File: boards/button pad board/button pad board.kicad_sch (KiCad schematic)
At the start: 4 parts

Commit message: button schematic work
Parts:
- added D1: LED_RBGA, LED_SMD:LED_RGB_5050-6, symbol Device:LED_RBGA
- U1: Mouser (none) -> 474-COM-07836
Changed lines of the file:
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@@
+      (effects (font (size 1.27 1.27)) hide)
+    )
+    (property "Mouser" "474-COM-07836 " (at 57.15 39.37 0)
       (effects (font (size 1.27 1.27)) hide)
     )
@@
       (effects (font (size 1.27 1.27)) hide)
     )
+    (property "Mouser" "474-COM-07836 " (at 30.48 39.37 0)
+      (effects (font (size 1.27 1.27)) hide)
+    )
     (pin "B1")
     (pin "G1")
@@
       (effects (font (size 1.27 1.27)) hide)
     )
+    (property "Mouser" "474-COM-07836 " (at 29.21 74.93 0)
+      (effects (font (size 1.27 1.27)) hide)
+    )
     (pin "B1")
     (pin "G1")
@@
       (effects (font (size 1.27 1.27)) hide)
     )
+    (property "Mouser" "474-COM-07836 " (at 55.88 74.93 0)
+      (effects (font (size 1.27 1.27)) hide)
+    )
     (pin "B1")
     (pin "G1")
@@
         )
       )
+    )
+  )
+  (symbol (lib_id "Device:LED_RBGA") (at 52.07 129.54 0) (unit 1)
+    (in_bom yes) (on_board yes) (dnp no) (fields_autoplaced)
+    (property "Reference" "D1" (at 52.07 116.84 0)
+      (effects (font (size 1.27 1.27)))
+    )
+    (property "Value" "LED_RBGA" (at 52.07 119.38 0)
+      (effects (font (size 1.27 1.27)))
+    )
+    (property "Footprint" "LED_SMD:LED_RGB_5050-6" (at 52.07 130.81 0)
+      (effects (font (size 1.27 1.27)) hide)
+    )
+    (property "Datasheet" "~" (at 52.07 130.81 0)
+      (effects (font (size 1.27 1.27)) hide)
+    )
+    (property "LCSC" "C784540" (at 52.07 129.54 0)
+      (effects (font (size 1.27 1.27)) hide)
+    )
+    (pin "1")
+    (pin "2")
+    (pin "3")
+    (pin "4")
+    (instances
+      (project "button pad board"
+        (path "/66d98af2-097e-4f68-99f2-351c9b9568f9"
+          (reference "D1") (unit 1)
+        )
+      )

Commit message: worked on the button board a bit
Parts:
- D1: footprint LED_SMD:LED_RGB_5050-6 -> yarrboard:WURTH_LED_RGB_5050-6; symbol Device:LED_RBGA -> yarrboard:LED_RGB; Mouser (none) -> 710-150505M173300
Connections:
- net B0: now also D1.BK
- net G0: now also D1.GK
- net R0: now also D1.RK
- net VCC: now also D1.BA, D1.GA, D1.RA
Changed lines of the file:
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@@
 (kicad_sch (version 20230121) (generator eeschema)
   (paper "A4")
+  (junction (at 60.96 123.19) (diameter 0) (color 0 0 0 0)
+  )
+  (junction (at 60.96 128.27) (diameter 0) (color 0 0 0 0)
+  )
+  (wire (pts (xy 60.96 123.19) (xy 60.96 128.27))
+    (stroke (width 0) (type default))
+  )
   (wire (pts (xy 238.76 71.12) (xy 238.76 74.93))
     (stroke (width 0) (type default))
@@
     (stroke (width 0) (type default))
   )
+  (wire (pts (xy 58.42 123.19) (xy 60.96 123.19))
+    (stroke (width 0) (type default))
+  )
   (wire (pts (xy 238.76 74.93) (xy 234.95 74.93))
     (stroke (width 0) (type default))
@@
     (stroke (width 0) (type default))
   )
+  (wire (pts (xy 44.45 128.27) (xy 48.26 128.27))
+    (stroke (width 0) (type default))
+  )
   (wire (pts (xy 119.38 53.34) (xy 121.92 53.34))
     (stroke (width 0) (type default))
@@
     (stroke (width 0) (type default))
   )
+  (wire (pts (xy 60.96 128.27) (xy 58.42 128.27))
+    (stroke (width 0) (type default))
+  )
+  (wire (pts (xy 60.96 133.35) (xy 60.96 128.27))
+    (stroke (width 0) (type default))
+  )
+  (wire (pts (xy 44.45 133.35) (xy 48.26 133.35))
+    (stroke (width 0) (type default))
+  )
   (wire (pts (xy 154.94 35.56) (xy 154.94 39.37))
     (stroke (width 0) (type default))
@@
     (stroke (width 0) (type default))
   )
+  (wire (pts (xy 44.45 123.19) (xy 48.26 123.19))
+    (stroke (width 0) (type default))
+  )
   (wire (pts (xy 209.55 53.34) (xy 212.09 53.34))
     (stroke (width 0) (type default))
@@
     (stroke (width 0) (type default))
   )
+  (wire (pts (xy 60.96 120.65) (xy 60.96 123.19))
+    (stroke (width 0) (type default))
+  )
   (wire (pts (xy 96.52 39.37) (xy 92.71 39.37))
     (stroke (width 0) (type default))
@@
     (stroke (width 0) (type default))
   )
+  (wire (pts (xy 58.42 133.35) (xy 60.96 133.35))
+    (stroke (width 0) (type default))
+  )
   (wire (pts (xy 181.61 39.37) (xy 177.8 39.37))
     (stroke (width 0) (type default))
@@
     )
   )
+  (global_label "G0" (shape input) (at 44.45 128.27 180) (fields_autoplaced)
+    (effects (font (size 1.27 1.27)) (justify right))
+    (property "Intersheetrefs" "${INTERSHEET_REFS}" (at 38.9853 128.27 0)
+      (effects (font (size 1.27 1.27)) (justify right) hide)
+    )
+  )
   (global_label "IN1" (shape input) (at 167.64 53.34 180) (fields_autoplaced)
     (effects (font (size 1.27 1.27)) (justify right))
@@
     )
   )
+  (global_label "B0" (shape input) (at 44.45 133.35 180) (fields_autoplaced)
+    (effects (font (size 1.27 1.27)) (justify right))
+    (property "Intersheetrefs" "${INTERSHEET_REFS}" (at 38.9853 133.35 0)
+      (effects (font (size 1.27 1.27)) (justify right) hide)
+    )
+  )
   (global_label "G1" (shape input) (at 226.06 39.37 180) (fields_autoplaced)
     (effects (font (size 1.27 1.27)) (justify right))
@@
     (effects (font (size 1.27 1.27)) (justify right))
     (property "Intersheetrefs" "${INTERSHEET_REFS}" (at 135.5053 34.29 0)
+      (effects (font (size 1.27 1.27)) (justify right) hide)
+    )
+  )
+  (global_label "R0" (shape input) (at 44.45 123.19 180) (fields_autoplaced)
+    (effects (font (size 1.27 1.27)) (justify right))
+    (property "Intersheetrefs" "${INTERSHEET_REFS}" (at 38.9853 123.19 0)
       (effects (font (size 1.27 1.27)) (justify right) hide)
     )
@@
     )
   )
+  (symbol (lib_id "power:VCC") (at 60.96 120.65 0) (unit 1)
+    (in_bom yes) (on_board yes) (dnp no) (fields_autoplaced)
+    (property "Reference" "#PWR033" (at 60.96 124.46 0)
+      (effects (font (size 1.27 1.27)) hide)
+    )
+    (property "Value" "VCC" (at 60.96 115.57 0)
+      (effects (font (size 1.27 1.27)))
+    )
+    (property "Footprint" "" (at 60.96 120.65 0)
+      (effects (font (size 1.27 1.27)) hide)
+    )
+    (property "Datasheet" "" (at 60.96 120.65 0)
+      (effects (font (size 1.27 1.27)) hide)
+    )
+    (pin "1")
+    (instances
+      (project "button pad board"
+        (path "/66d98af2-097e-4f68-99f2-351c9b9568f9"
+          (reference "#PWR033") (unit 1)
+        )
+      )
+    )
+  )
   (symbol (lib_name "2x2_RGB_Button_1") (lib_id "yarrboard:2x2_RGB_Button") (at 87.63 39.37 0) (unit 1)
     (in_bom yes) (on_board yes) (dnp no) (fields_autoplaced)
@@
     )
   )
-  (symbol (lib_id "Device:LED_RBGA") (at 52.07 129.54 0) (unit 1)
-    (in_bom yes) (on_board yes) (dnp no) (fields_autoplaced)
-    (property "Reference" "D1" (at 52.07 116.84 0)
-      (effects (font (size 1.27 1.27)))
-    )
-    (property "Value" "LED_RBGA" (at 52.07 119.38 0)
-      (effects (font (size 1.27 1.27)))
-    )
-    (property "Footprint" "LED_SMD:LED_RGB_5050-6" (at 52.07 130.81 0)
-      (effects (font (size 1.27 1.27)) hide)
-    )
-    (property "Datasheet" "~" (at 52.07 130.81 0)
-      (effects (font (size 1.27 1.27)) hide)
-    )
-    (property "LCSC" "C784540" (at 52.07 129.54 0)
-      (effects (font (size 1.27 1.27)) hide)
-    )
-    (pin "1")
-    (pin "2")
-    (pin "3")
-    (pin "4")
-    (instances
-      (project "button pad board"
+  (symbol (lib_id "yarrboard:LED_RGB") (at 53.34 128.27 0) (unit 1)
+    (in_bom yes) (on_board yes) (dnp no) (fields_autoplaced)
+    (property "Reference" "D1" (at 53.34 115.57 0)
+      (effects (font (size 1.27 1.27)))
+    )
+    (property "Value" "LED_RBGA" (at 53.34 118.11 0)
+      (effects (font (size 1.27 1.27)))
+    )
+    (property "Footprint" "yarrboard:WURTH_LED_RGB_5050-6" (at 53.34 129.54 0)
+      (effects (font (size 1.27 1.27)) hide)
+    )
+    (property "Datasheet" "~" (at 53.34 129.54 0)
+      (effects (font (size 1.27 1.27)) hide)
+    )
+    (property "LCSC" "C784540" (at 53.34 128.27 0)
+      (effects (font (size 1.27 1.27)) hide)
+    )
+    (property "Mouser" " 710-150505M173300 " (at 53.34 128.27 0)
+      (effects (font (size 1.27 1.27)) hide)
+    )
+    (pin "BA")
+    (pin "BK")
+    (pin "GA")
+    (pin "GK")
+    (pin "RA")
+    (pin "RK")
+    (instances
+      (project "button pad board"

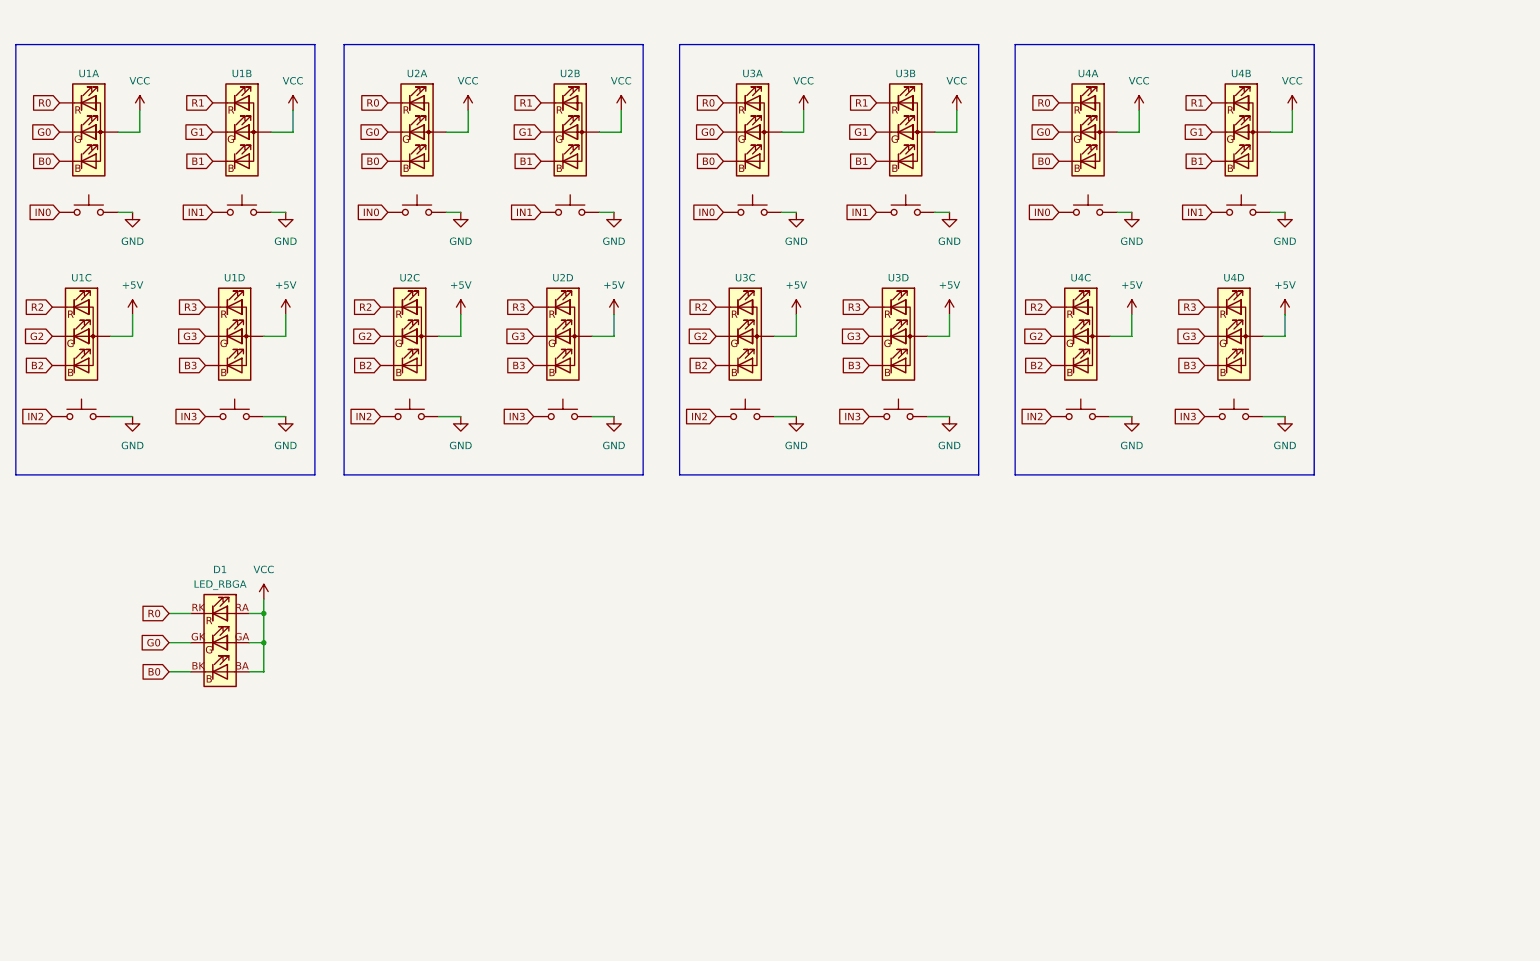
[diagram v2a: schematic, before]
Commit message: changed to 5050 led for interface board
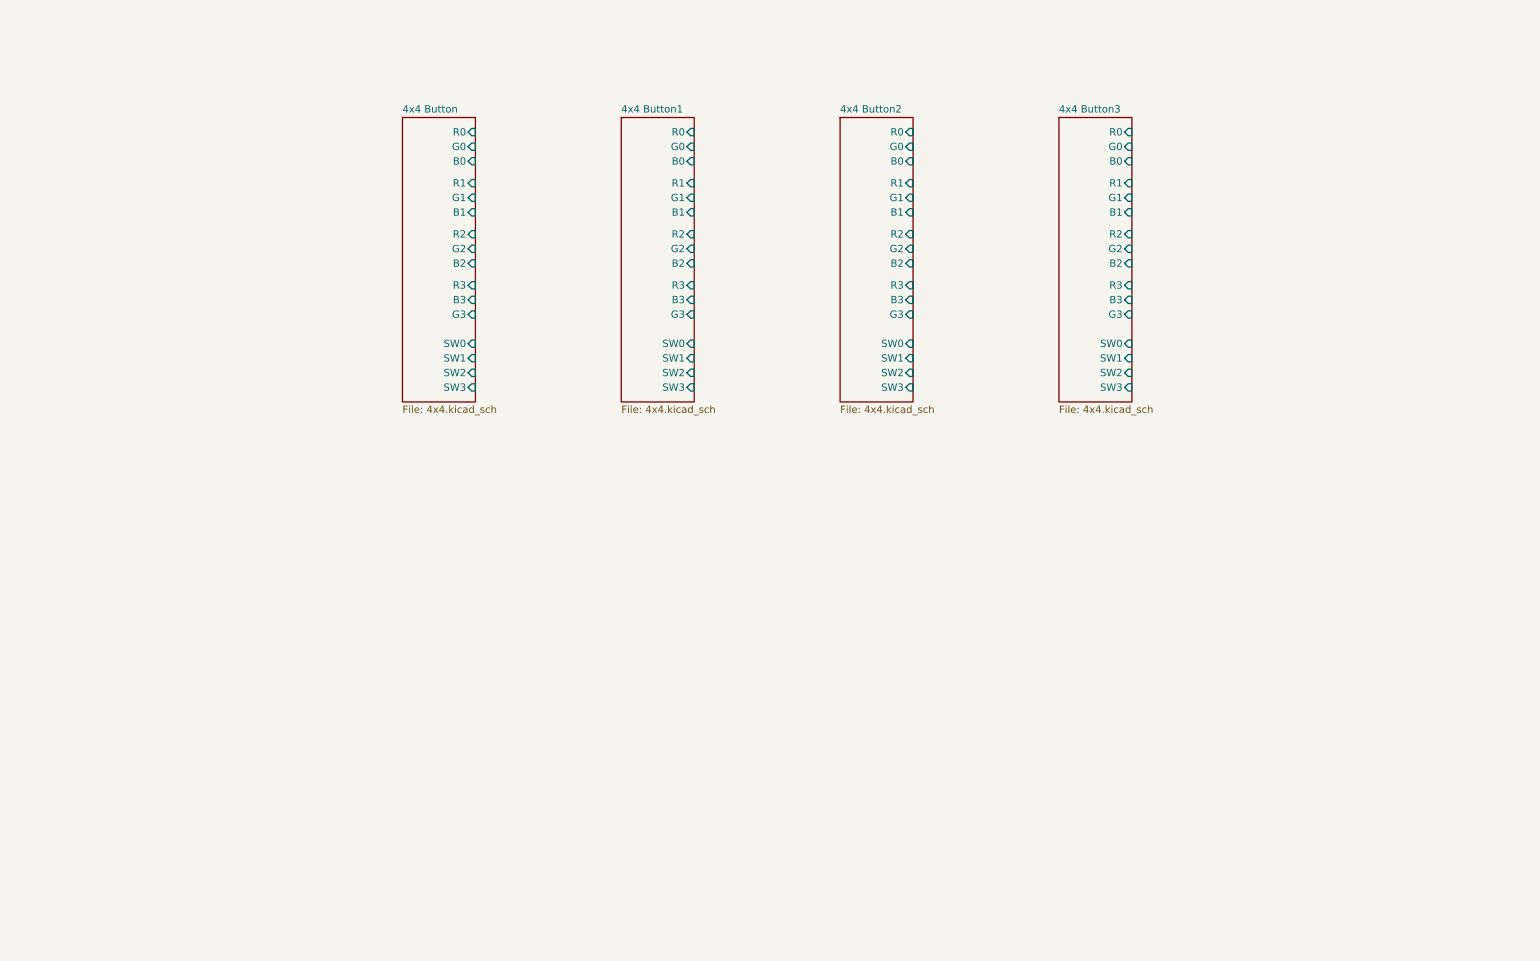
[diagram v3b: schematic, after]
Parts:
- removed D1: LED_RBGA, yarrboard:WURTH_LED_RGB_5050-6, symbol yarrboard:LED_RGB
- removed U1, U2, U3, U4: ~, yarrboard:BUTTONPAD-2X2, symbol yarrboard:2x2_RGB_Button
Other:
- added sheet 4x4 Button (4x4.kicad_sch)
- added sheet 4x4 Button1 (4x4.kicad_sch)
- added sheet 4x4 Button2 (4x4.kicad_sch)
- added sheet 4x4 Button3 (4x4.kicad_sch)

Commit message: good progress on teh button board
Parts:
- added J1: RGB, Connector_IDC:IDC-Header_2x25_P2.54mm_Horizontal, symbol Connector_Generic:Conn_02x25_Odd_Even
- added J2: INPUTS, Connector_IDC:IDC-Header_2x10_P2.54mm_Horizontal, symbol Connector_Generic:Conn_02x10_Odd_Even
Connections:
- new net +3V3: J2.1 (Pin_1), J2.3 (Pin_3)
- new net +5V: J1.1 (Pin_1)
- new net B0: J1.12 (Pin_12)
- new net B1: J1.9 (Pin_9)
- new net B10: J1.35 (Pin_35)
- new net B11: J1.38 (Pin_38)
- new net B12: J1.48 (Pin_48)
- new net B13: J1.45 (Pin_45)
- new net B14: J1.42 (Pin_42)
- new net B15: J1.39 (Pin_39)
- new net B2: J1.6 (Pin_6)
- new net B3: J1.3 (Pin_3)
- new net B4: J1.17 (Pin_17)
- new net B5: J1.20 (Pin_20)
- new net B6: J1.23 (Pin_23)
- new net B7: J1.26 (Pin_26)
- new net B8: J1.29 (Pin_29)
- new net B9: J1.32 (Pin_32)
- new net G0: J1.13 (Pin_13)
- new net G1: J1.10 (Pin_10)
- new net G10: J1.34 (Pin_34)
- new net G11: J1.37 (Pin_37)
- new net G12: J1.49 (Pin_49)
- new net G13: J1.46 (Pin_46)
- new net G14: J1.43 (Pin_43)
- new net G15: J1.40 (Pin_40)
- new net G2: J1.7 (Pin_7)
- new net G3: J1.4 (Pin_4)
- new net G4: J1.16 (Pin_16)
- new net G5: J1.19 (Pin_19)
- new net G6: J1.22 (Pin_22)
- new net G7: J1.25 (Pin_25)
- new net G8: J1.28 (Pin_28)
- new net G9: J1.31 (Pin_31)
- new net GND: J1.2 (Pin_2), J2.2 (Pin_2), J2.4 (Pin_4)
- new net R0: J1.14 (Pin_14)
- new net R1: J1.11 (Pin_11)
- new net R10: J1.33 (Pin_33)
- new net R11: J1.36 (Pin_36)
- new net R12: J1.50 (Pin_50)
- new net R13: J1.47 (Pin_47)
- new net R14: J1.44 (Pin_44)
- new net R15: J1.41 (Pin_41)
- new net R2: J1.8 (Pin_8)
- new net R3: J1.5 (Pin_5)
- new net R4: J1.15 (Pin_15)
- new net R5: J1.18 (Pin_18)
- new net R6: J1.21 (Pin_21)
- new net R7: J1.24 (Pin_24)
- new net R8: J1.27 (Pin_27)
- new net R9: J1.30 (Pin_30)
- new net SW0: J2.5 (Pin_5)
- new net SW1: J2.6 (Pin_6)
- new net SW10: J2.15 (Pin_15)
- new net SW11: J2.16 (Pin_16)
- new net SW12: J2.17 (Pin_17)
- new net SW13: J2.18 (Pin_18)
- new net SW14: J2.19 (Pin_19)
- new net SW15: J2.20 (Pin_20)
- new net SW2: J2.7 (Pin_7)
- new net SW3: J2.8 (Pin_8)
- new net SW4: J2.9 (Pin_9)
- new net SW5: J2.10 (Pin_10)
- new net SW6: J2.11 (Pin_11)
- new net SW7: J2.12 (Pin_12)
- new net SW8: J2.13 (Pin_13)
- new net SW9: J2.14 (Pin_14)

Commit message: button board updated, routed, and ready to rock.
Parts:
- removed J1: RGB, Connector_IDC:IDC-Header_2x25_P2.54mm_Horizontal, symbol Connector_Generic:Conn_02x25_Odd_Even
- removed J2: INPUTS, Connector_IDC:IDC-Header_2x10_P2.54mm_Horizontal, symbol Connector_Generic:Conn_02x10_Odd_Even
- added H1, H2, H3, H4: MountingHole, MountingHole:MountingHole_3.2mm_M3_DIN965_Pad, symbol Mechanical:MountingHole_Pad
- added J1: RGB, Connector_FFC-FPC:TE_3-84952-0_1x30-1MP_P1.0mm_Horizontal, symbol Connector_Generic_MountingPin:Conn_01x30_MountingPin
- added J3: INPUTS, Connector_FFC-FPC:TE_1-84952-0_1x10-1MP_P1.0mm_Horizontal, symbol Connector_Generic_MountingPin:Conn_01x10_MountingPin
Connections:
- net +5V: now also J1.1 (Pin_1), J1.2 (Pin_2), J1.3 (Pin_3)
- net B0: now also J1.9 (Pin_9)
- net B1: now also J1.12 (Pin_12)
- net B2: now also J1.15 (Pin_15)
- net B3: now also J1.18 (Pin_18)
- net B4: now also J1.21 (Pin_21)
- net B5: now also J1.24 (Pin_24)
- net B6: now also J1.27 (Pin_27)
- net B7: now also J1.30 (Pin_30)
- net G0: now also J1.8 (Pin_8)
- net G1: now also J1.11 (Pin_11)
- net G2: now also J1.14 (Pin_14)
- net G3: now also J1.17 (Pin_17)
- net G4: now also J1.20 (Pin_20)
- net G5: now also J1.23 (Pin_23)
- net G6: now also J1.26 (Pin_26)
- net G7: now also J1.29 (Pin_29)
- net GND: now also H1.1, H2.1, H3.1, H4.1, J1.4 (Pin_4), J1.5 (Pin_5), J1.6 (Pin_6), J1.MP (MountPin), J3.2 (Pin_2), J3.MP (MountPin)
- net R0: now also J1.7 (Pin_7)
- net R1: now also J1.10 (Pin_10)
- net R2: now also J1.13 (Pin_13)
- net R3: now also J1.16 (Pin_16)
- net R4: now also J1.19 (Pin_19)
- net R5: now also J1.22 (Pin_22)
- net R6: now also J1.25 (Pin_25)
- net R7: now also J1.28 (Pin_28)
- net SW0: now also J3.3 (Pin_3)
- net SW1: now also J3.4 (Pin_4)
- net SW2: now also J3.5 (Pin_5)
- net SW3: now also J3.6 (Pin_6)
- net SW4: now also J3.7 (Pin_7)
- net SW5: now also J3.8 (Pin_8)
- net SW6: now also J3.9 (Pin_9)
- net SW7: now also J3.10 (Pin_10)
- new net +3.3V: J3.1 (Pin_1)
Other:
- removed sheet 4x4 Button2
- removed sheet 4x4 Button3
- company: (none) -> github.com/hoeken/yarrboard
- title: (none) -> RGB Button Pad Board
